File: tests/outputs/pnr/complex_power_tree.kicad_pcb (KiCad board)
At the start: 6 copper layers, 55 x 55 mm, 48 parts

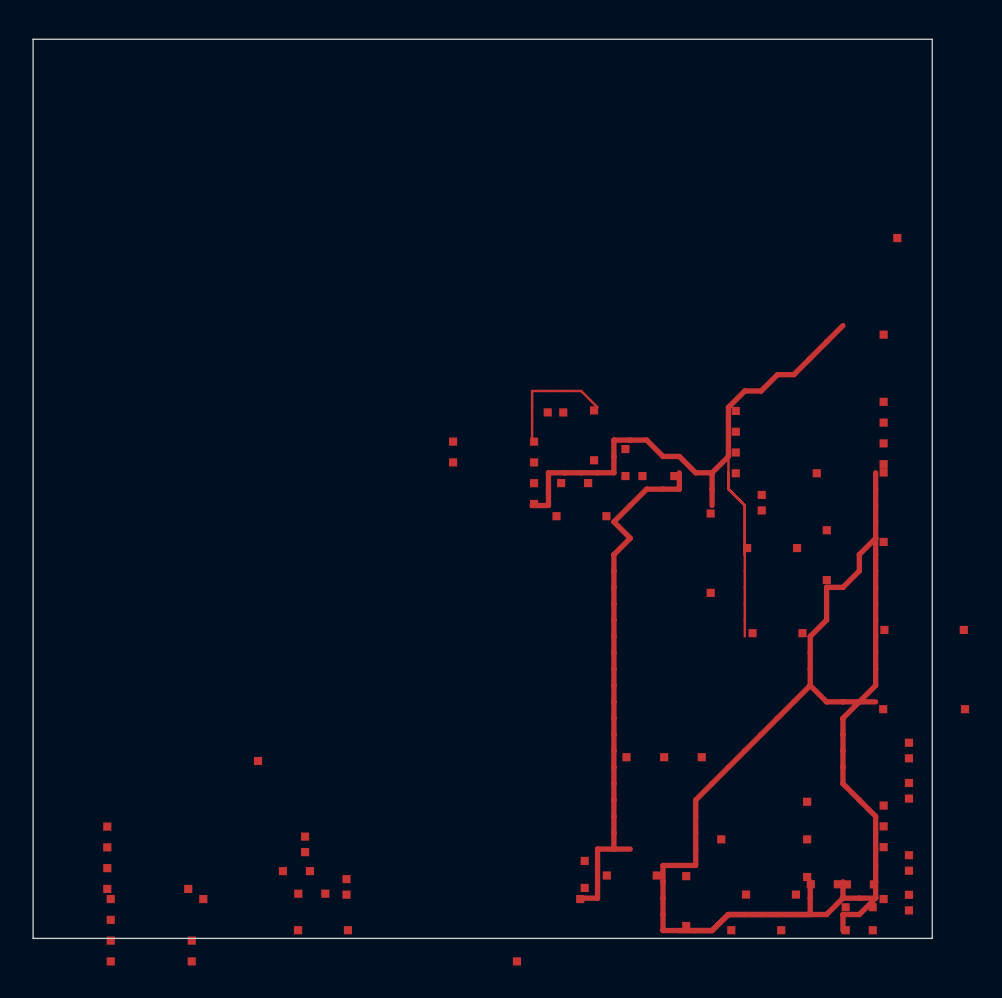
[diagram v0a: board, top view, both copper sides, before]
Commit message: fix: filter power symbols, realistic pads, routing clearance
- Filter power/ground symbol instances from PnR board. Only instances
  with component_class attribute (set by synthesizer) are physical
  components. Reduces 48 → 30 real components.
- Use actual IPC-7351B pad dimensions (width × height) in HTML
  visualization instead of fixed 0.5mm dots.
- Add min_spacing_mm clearance around component footprints in the
  routing grid to prevent traces from going through components.
- Improve component category detection for HTML color coding.

Co-Authored-By: Claude Opus 4.6 (1M context) <noreply@anthropic.com>
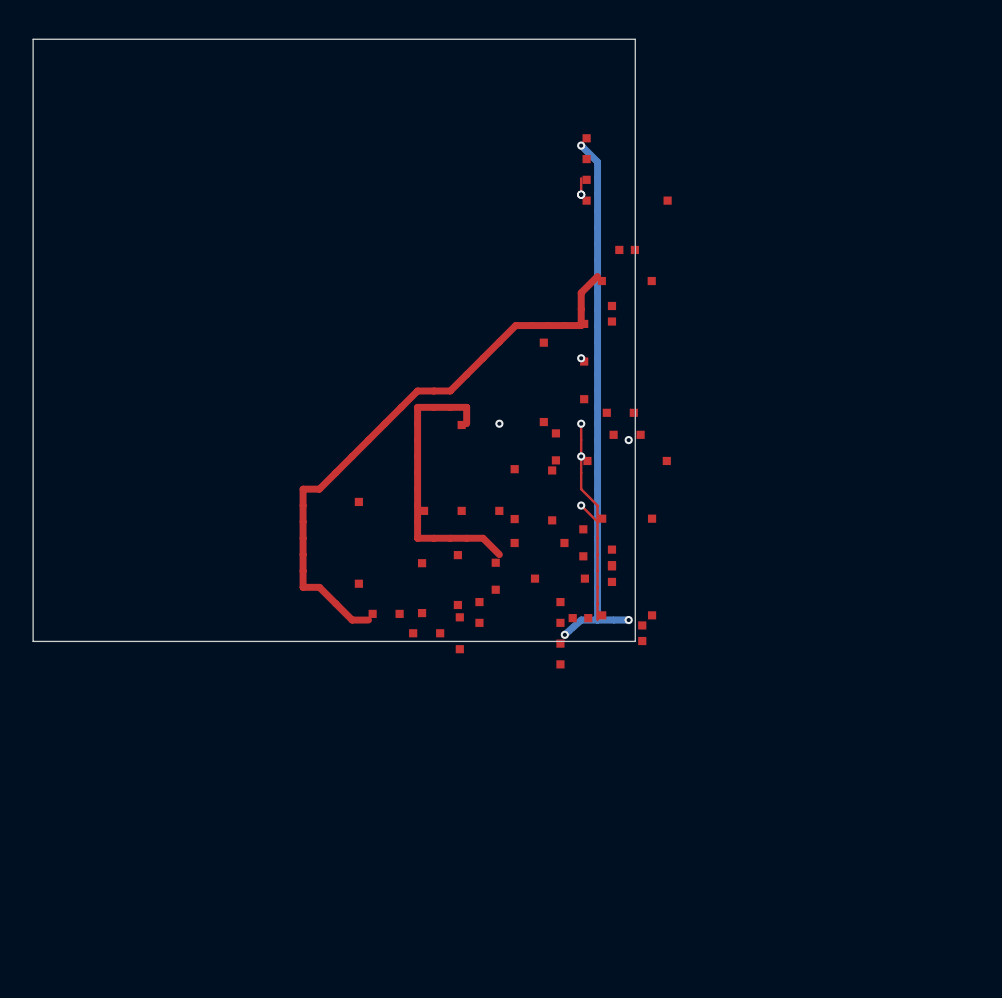
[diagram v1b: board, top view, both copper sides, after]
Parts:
- removed C10: , 1206
- removed D7, D8: , SOT-23
- removed L3: , 0805
- removed R10: , 0603
- removed U10, U11, U12, U13, U3, U4, U5, U6, U7, U8, U9: , SOIC-8
- removed U14, U15: , SOT-223
- C1: footprint 0603 -> 1206
- C2: footprint 1206 -> 2010
- C3: footprint 2010 -> 1206
- L2: footprint 1210 -> 0805
- R2: footprint 0603 -> THT
- R3: footprint THT -> 0603
- R6: footprint 0603 -> 2010
- R7: footprint 2010 -> 0603
- U1, U2: footprint SOIC-8 -> SOT-223
- moved D4 42.5 mm to (36.3, 12.0), turned to 90 degrees
- moved U1 36.2 mm to (26.2, 26.2), turned to 90 degrees
- moved R2 35.3 mm to (19.9, 30.8), turned to 90 degrees
- moved R4 34.9 mm to (32.0, 24.9), turned to 90 degrees
- moved R5 34.0 mm to (21.6, 35.1)
- moved R1 33.5 mm to (36.3, 24.2), turned to 180 degrees
- moved R8 32.4 mm to (35.9, 22.8)
- moved L1 31.3 mm to (36.3, 29.3)
- moved C5 28.1 mm to (26.0, 33.1), turned to 90 degrees
- moved R3 27.4 mm to (28.3, 32.8), turned to 90 degrees
- moved D5 27.1 mm to (36.3, 32.7)
- moved D2 25.7 mm to (36.3, 31.7)
- moved R6 25.4 mm to (36.3, 25.8), turned to 360 degrees
- moved C6 23.2 mm to (32.2, 33.0), turned to 0 degrees
- moved D1 22.4 mm to (36.3, 36.3), turned to 180 degrees
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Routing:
- net 0: track 180.0 -> 148.6 mm, vias 0 -> 11
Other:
- board size 55 x 55 mm -> 36.8 x 36.8 mm

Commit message: fix: use full footprint extent for component outlines
Compute component width/height from the full footprint extent
(body + pad protrusion) instead of just the IC body dimensions.
This ensures pads are always inside the component outline.

Use all IPC-7351B footprint pads as pin positions (authoritative
source) instead of matching to module pin count. SOT-23 now has
3 pins, SOIC-8 has 8, etc.

Updated dimensions:
  SOT-23: 2.9×1.3mm → 3.2×1.5mm (includes lead protrusion)
  SOIC-8: 4.9×3.9mm → 6.8×4.3mm (includes lead protrusion)
  0603:   1.6×0.8mm → 2.4×0.9mm (includes pad overhang)

Board auto-sizes to 44×44mm for 30 real components (was 55×55
for 48 including power symbols).

Co-Authored-By: Claude Opus 4.6 (1M context) <noreply@anthropic.com>
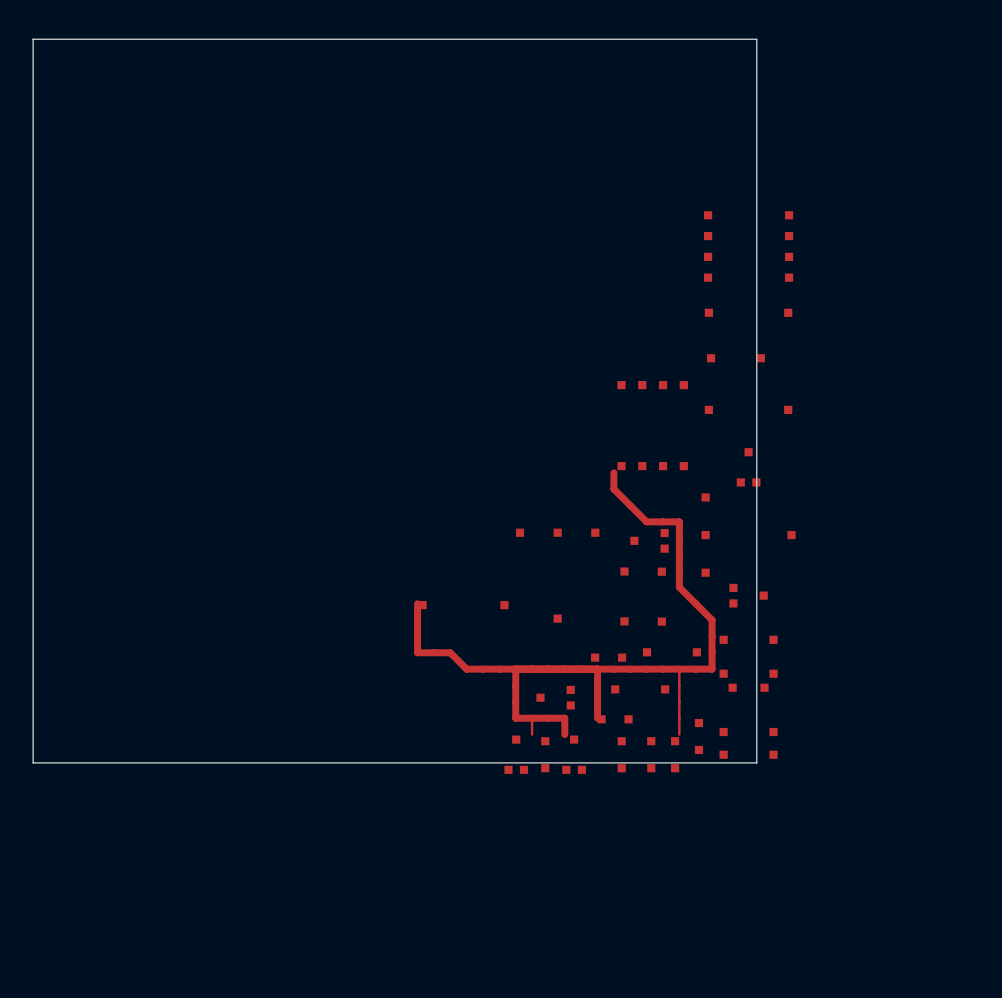
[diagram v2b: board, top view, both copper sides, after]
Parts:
- moved D4 28.6 mm to (31.9, 40.2), turned to 180 degrees
- moved D3 27.8 mm to (29.5, 43.7), turned to 90 degrees
- moved C8 23.2 mm to (43.7, 36.7)
- moved R8 20.9 mm to (36.0, 43.7), turned to 90 degrees
- moved C1 20.6 mm to (43.7, 38.8), turned to 360 degrees
- moved R4 18.8 mm to (31.3, 43.7), turned to 270 degrees
- moved L2 18.0 mm to (43.7, 39.6), turned to 0 degrees
- moved R9 17.8 mm to (40.7, 42.6), turned to 270 degrees
- moved R1 17.4 mm to (35.6, 41.6), turned to 360 degrees
- moved L1 16.2 mm to (43.7, 43.7), turned to 180 degrees
- moved C4 15.9 mm to (43.0, 19.5), turned to 360 degrees
- moved R3 15.5 mm to (39.2, 43.7), turned to 270 degrees
- moved X2 15.1 mm to (37.9, 23.6), turned to 270 degrees
- moved R5 13.9 mm to (35.2, 37.8)
- moved R7 13.6 mm to (37.8, 43.7)
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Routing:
- net 0: track 148.6 -> 71.1 mm, vias 11 -> 0
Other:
- board size 36.8 x 36.8 mm -> 44.2 x 44.2 mm

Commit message: feat: center-out placement with progressive freezing
Major placement improvements:
- Most-connected component placed at board center as anchor
- BFS spiral placement: neighbors placed radially around anchor
- Progressive freezing: components that stabilize for 50 iterations
  get frozen, becoming obstacles for remaining placement
- Anchor is always frozen (never moves)
- Adam optimizer skips frozen components

Fix board boundary enforcement:
- Component clamping accounts for component half-width/half-height
  so edges stay inside the board outline
- Legalization overlap resolver also respects component size
- Board auto-sizing uses 4× multiplier with 50mm minimum

Fix power symbol filtering:
- Use component_class attribute as the reliable signal
  (only instances with component_class are physical)
- Footprint extent includes pad protrusion (not just IC body)
- All IPC-7351B pads used as pin positions (authoritative source)

Fix sort panic: BFS neighbor ordering uses deterministic
hash-based tie-breaking instead of random comparator.

Stronger density force (lambda_density: 0.5 → 2.0).

Co-Authored-By: Claude Opus 4.6 (1M context) <noreply@anthropic.com>
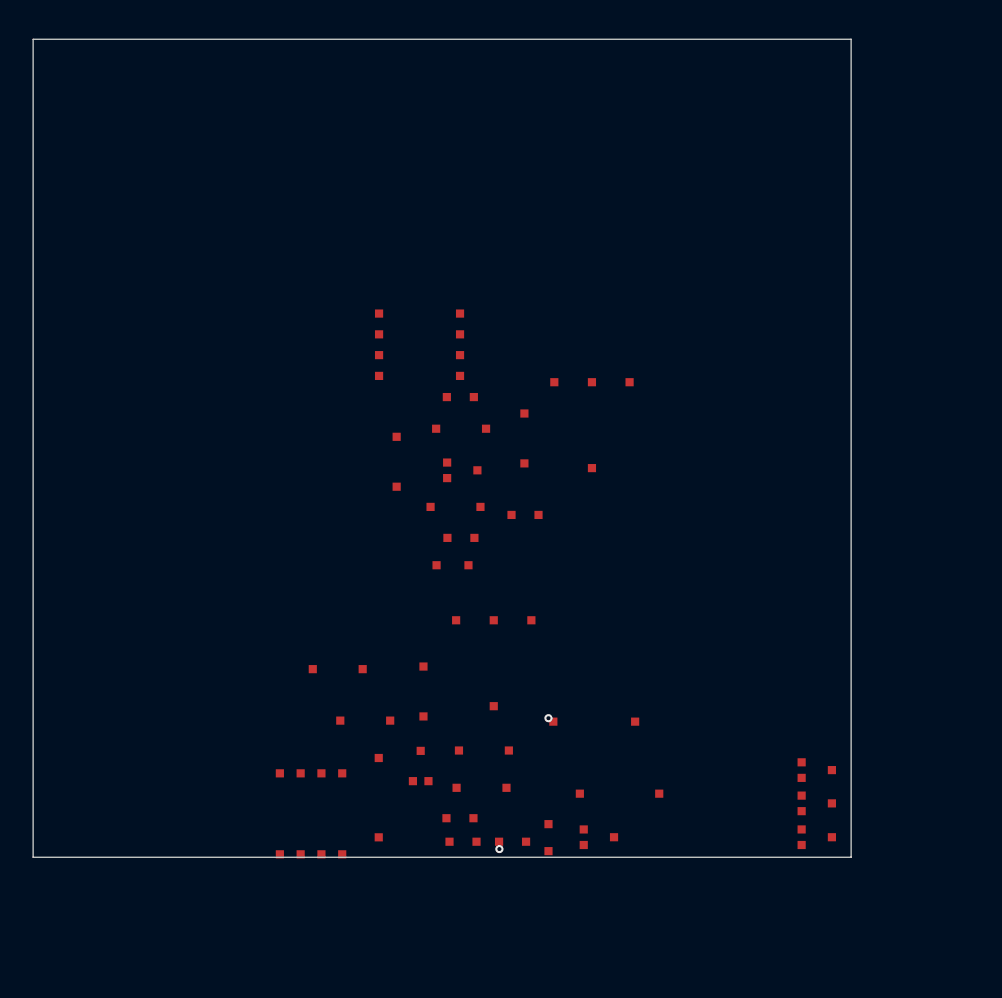
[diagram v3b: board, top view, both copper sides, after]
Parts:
- moved X1 43.8 mm to (17.0, 47.3), turned to 90 degrees
- moved C2 37.3 mm to (21.1, 46.4), turned to 90 degrees
- moved C4 28.5 mm to (27.6, 43.5)
- moved L1 25.7 mm to (18.6, 38.5), turned to 0 degrees
- moved R9 25.4 mm to (26.1, 21.9), turned to 0 degrees
- moved R6 24.7 mm to (35.8, 46.1)
- moved C3 23.4 mm to (20.3, 41.6)
- moved C8 21.8 mm to (26.2, 23.8)
- moved D5 21.0 mm to (47.9, 46.7), turned to 0 degrees
- moved C6 20.5 mm to (22.2, 25.8), turned to 270 degrees
- moved C1 19.9 mm to (23.9, 39.9), turned to 270 degrees
- moved L2 19.6 mm to (25.6, 32.2)
- moved D6 19.1 mm to (26.2, 26.3)
- moved D3 18.4 mm to (47.9, 44.7), turned to 0 degrees
- moved D2 18.4 mm to (34.6, 48.8), turned to 0 degrees
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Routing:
- net 0: track 71.1 -> 9.24 mm, vias 0 -> 2
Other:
- board size 44.2 x 44.2 mm -> 50 x 50 mm

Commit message: feat: ePlace-style density calibration and pairwise overlap repulsion
Major placement algorithm improvements:
- Auto-calibrate λ_density on first iteration so ||∇_WL|| ≈ ||λ_D·∇_D||
  (ePlace approach — forces balanced from the start)
- Grow λ_density by 1.02× every 10 iterations (ePlace lambda schedule)
- Quadratic density penalty: charge = excess · |excess| (stronger at
  high overlap, gentle at low overlap)
- Direct pairwise overlap repulsion O(n²) supplements FFT density
  (resolves individual overlaps the coarse grid can't distinguish)
- Mini-legalization every iteration: directly push overlapping
  components apart by 0.3mm/iter during optimization
- Gamma annealing from 2.0 → 0.1 (every 20 iterations × 0.9)
- Position lr: 2.0mm/step (was 0.5)
- Progressive freezer threshold: 200 iters (was 50)

Release build: 3 trials × 600 iterations = 10 seconds total.

Verification tool now integrated — reports overlaps, connection
lengths, group spread, and orientation issues after each run.

Co-Authored-By: Claude Opus 4.6 (1M context) <noreply@anthropic.com>
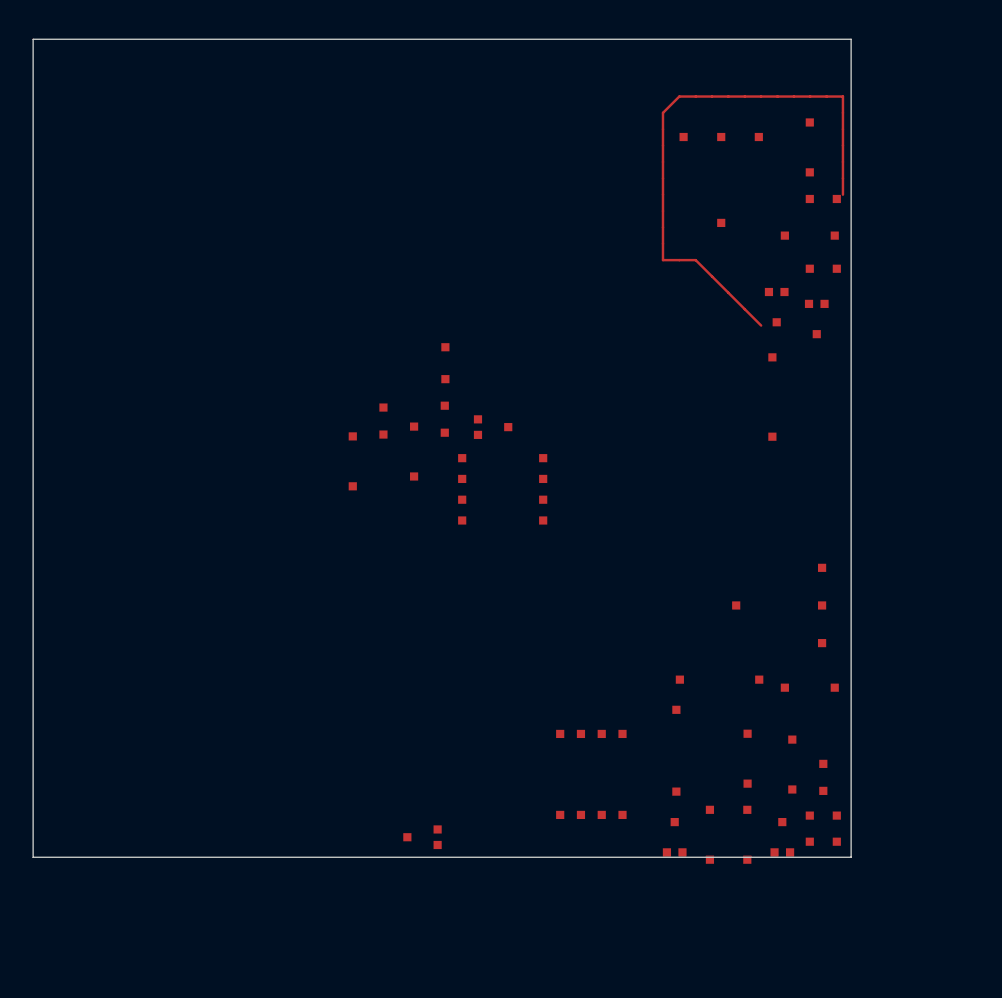
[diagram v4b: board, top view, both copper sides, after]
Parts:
- moved R7 38.6 mm to (48.3, 14.0), turned to 0 degrees
- moved D4 32.5 mm to (45.5, 16.4), turned to 270 degrees
- moved D5 29.6 mm to (47.9, 17.1), turned to 270 degrees
- moved R5 26.6 mm to (48.3, 9.76)
- moved R6 26.0 mm to (45.2, 21.9), turned to 90 degrees
- moved L1 25.6 mm to (43.7, 44.0), turned to 90 degrees
- moved C9 24.9 mm to (47.5, 6.61), turned to 90 degrees
- moved C3 24.4 mm to (43.7, 48.6), turned to 270 degrees
- moved C8 24.4 mm to (47.5, 12.0)
- moved C1 23.6 mm to (47.5, 39.6), turned to 360 degrees
- moved R4 22.4 mm to (48.3, 45.1), turned to 270 degrees
- moved R3 22.3 mm to (48.3, 49.0)
- moved C2 22.0 mm to (42.0, 39.1), turned to 0 degrees
- moved R1 19.1 mm to (48.3, 47.5)
- moved C4 18.9 mm to (46.4, 44.3), turned to 270 degrees
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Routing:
- net 0: track 9.24 -> 34.1 mm, vias 2 -> 0

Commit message: feat: spread-out initialization — components flung to board boundaries
Major placement breakthrough: initialize components spread across the
entire board in a grid, then let wirelength pull connected components
together while density/repulsion prevents overlap. This matches the
correct ePlace approach (converge from spread → tight, not tight → spread).

Key changes:
- BFS-ordered grid fills entire board (not clustered in one corner)
- Mini-legalization push proportional to overlap amount (was fixed 0.3mm)
- Position lr: 2.0mm/step for faster convergence

Results (3 trials, 600 iterations, release build: 3.3 seconds):
- Overlaps: 19 → 2 (nearly overlap-free!)
- 30/30 components inside board
- Groups cluster naturally: buck=13.5mm, reg33=10.9mm spread
- Components use full board area

Routability still low (7%) — routing grid blockage issue to fix next.

Co-Authored-By: Claude Opus 4.6 (1M context) <noreply@anthropic.com>
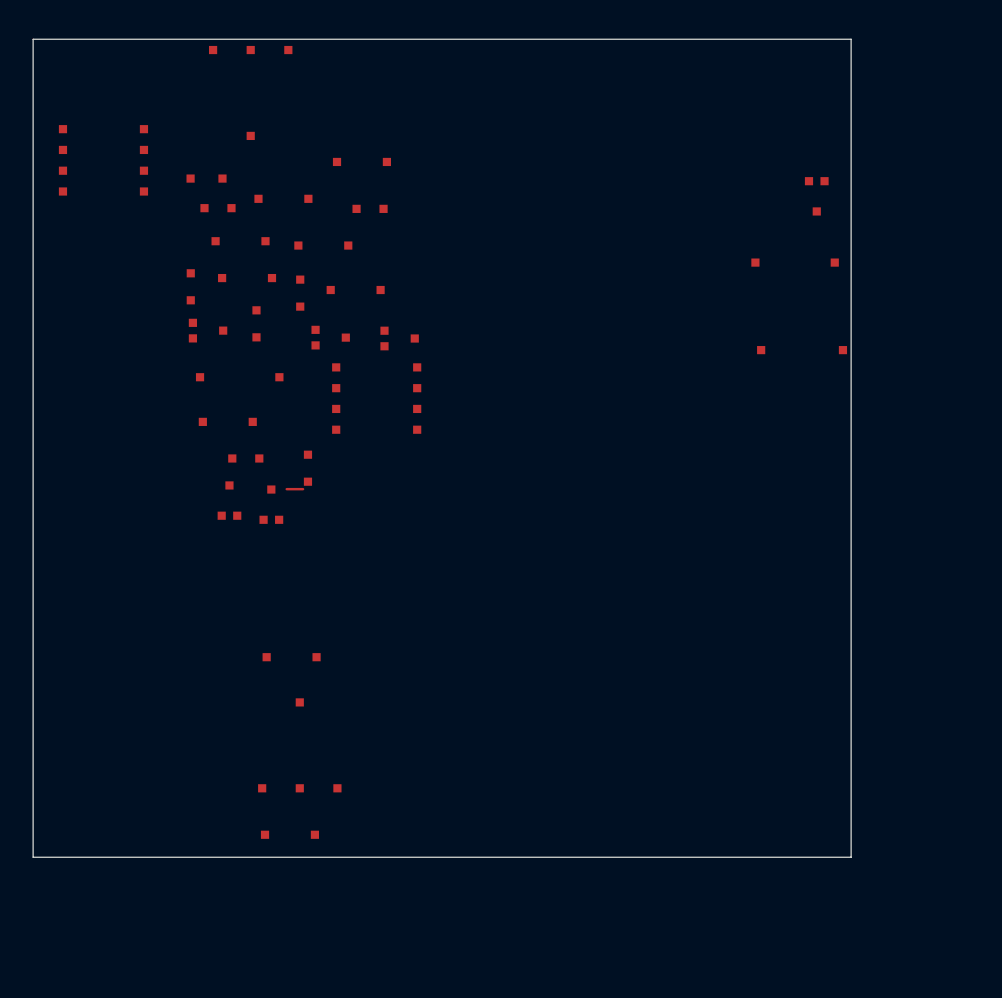
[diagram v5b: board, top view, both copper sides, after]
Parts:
- moved C3 48.1 mm to (15.3, 9.75), turned to 0 degrees
- moved R3 46.9 mm to (13.7, 17.4), turned to 270 degrees
- moved R1 46.3 mm to (20.6, 10.4), turned to 180 degrees
- moved R4 43.6 mm to (16.3, 15.5)
- moved C1 40.2 mm to (17.7, 12.6), turned to 180 degrees
- moved D2 40.1 mm to (47.9, 9.60), turned to 270 degrees
- moved D3 38.4 mm to (22.4, 18.3), turned to 0 degrees
- moved D5 37.6 mm to (12.0, 28.2), turned to 90 degrees
- moved L1 37.3 mm to (19.7, 15.3), turned to 0 degrees
- moved R7 37.2 mm to (13.0, 25.6), turned to 180 degrees
- moved R5 35.5 mm to (16.8, 26.2), turned to 90 degrees
- moved C2 34.7 mm to (12.6, 20.7)
- moved C8 34.5 mm to (13.1, 14.6)
- moved D4 33.2 mm to (14.6, 28.4), turned to 90 degrees
- moved X2 31.6 mm to (4.30, 7.40)
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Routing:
- net 0: track 34.1 -> 1.00 mm
